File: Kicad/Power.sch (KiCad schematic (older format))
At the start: 29 parts, among them J1 Conn_01x02_Male, J2 Jack-DC, Q1 Q_PMOS_DSG, Q2 Q_NMOS_DSG, U2 LM5155, U3 AMS1117-3.3

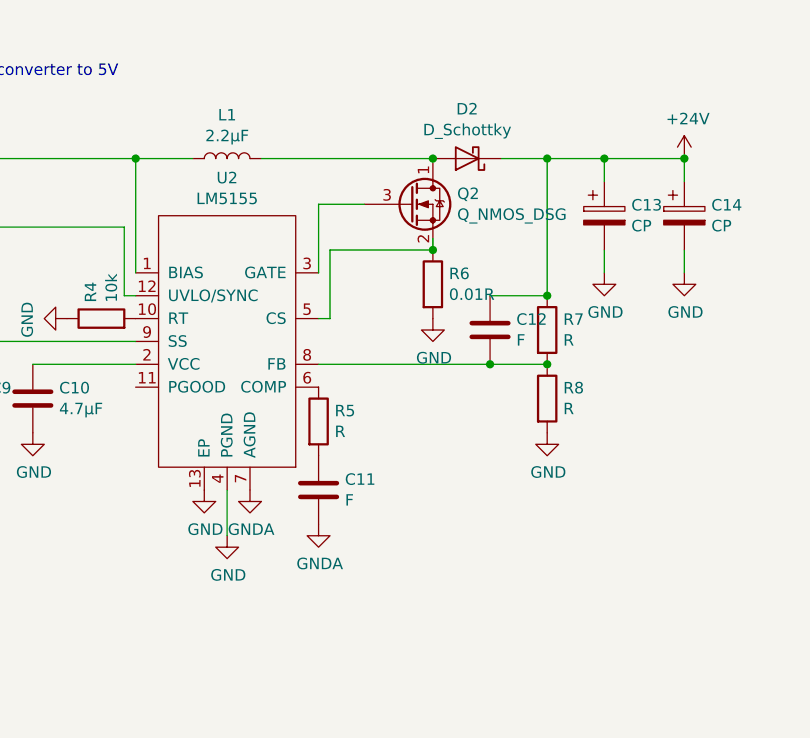
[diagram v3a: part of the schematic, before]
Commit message: Completed the TMC2130 layout and Boost converter layout
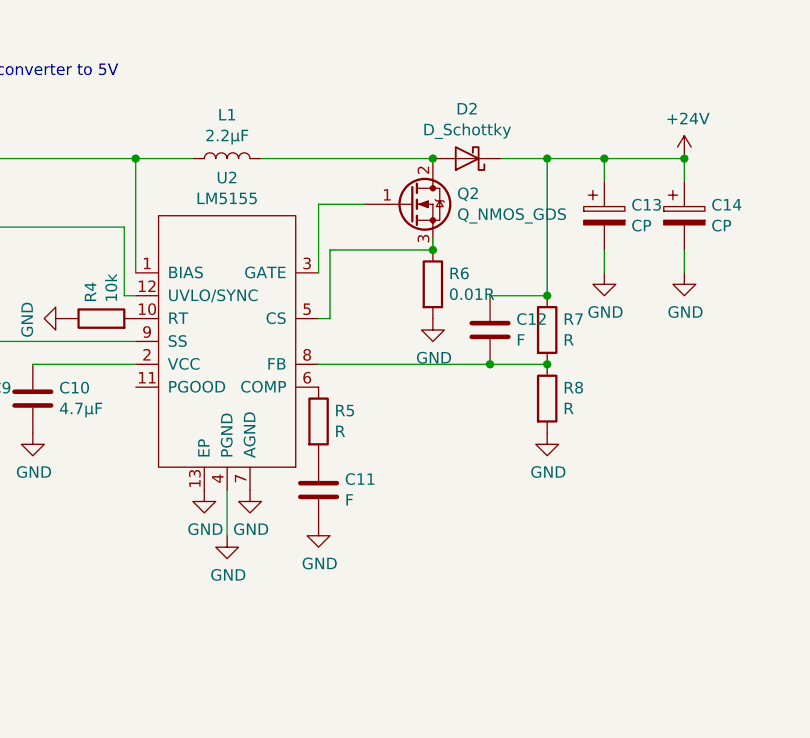
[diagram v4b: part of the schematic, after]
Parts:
- removed Q2: Q_NMOS_DSG, symbol Device:Q_NMOS_DSG
- added Q2: Q_NMOS_GDS, Package_TO_SOT_SMD:TO-252-2, symbol Device:Q_NMOS_GDS
- C10: footprint (none) -> Capacitor_SMD:C_0805_2012Metric
- C11, C12, C9: footprint (none) -> Capacitor_SMD:C_0603_1608Metric
- L1: footprint (none) -> PrivateLib:SRP1265A
- R2, R3, R4, R5, R7, R8: footprint (none) -> Resistor_SMD:R_0603_1608Metric
- R6: footprint (none) -> Resistor_SMD:R_1206_3216Metric
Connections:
- net GNDA is gone; now on net GND: C11.2, U2.7 (AGND)
- net at U2.3 (GATE): now also Q2.1 (G)
- net at R6.1, U2.5 (CS): now also Q2.3 (S)
- net at D2.2 (A), L1.2: now also Q2.2 (D)
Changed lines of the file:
@@
 F 0 "R2" H 4570 3646 50  0000 L CNN
 F 1 "R" H 4570 3555 50  0000 L CNN
-F 2 "" V 4430 3600 50  0001 C CNN
+F 2 "Resistor_SMD:R_0603_1608Metric" V 4430 3600 50  0001 C CNN
 F 3 "~" H 4500 3600 50  0001 C CNN
 	1    4500 3600
@@
 F 0 "R3" H 4570 3946 50  0000 L CNN
 F 1 "R" H 4570 3855 50  0000 L CNN
-F 2 "" V 4430 3900 50  0001 C CNN
+F 2 "Resistor_SMD:R_0603_1608Metric" V 4430 3900 50  0001 C CNN
 F 3 "~" H 4500 3900 50  0001 C CNN
 	1    4500 3900
@@
 F 0 "R4" H 5170 4196 50  0000 L CNN
 F 1 "10k" H 5170 4105 50  0000 L CNN
-F 2 "" V 5030 4150 50  0001 C CNN
+F 2 "Resistor_SMD:R_0603_1608Metric" V 5030 4150 50  0001 C CNN
 F 3 "~" H 5100 4150 50  0001 C CNN
 	1    5100 4150
@@
 F 0 "L1" V 5840 3450 50  0000 C CNN
 F 1 "2.2µF" V 5749 3450 50  0000 C CNN
-F 2 "" H 5650 3450 50  0001 C CNN
+F 2 "PrivateLib:SRP1265A" H 5650 3450 50  0001 C CNN
 F 3 "~" H 5650 3450 50  0001 C CNN
 	1    5650 3450
@@
 	5500 3450 5250 3450
 Connection ~ 5250 3450
-$Comp
-L Device:Q_NMOS_DSG Q2
-U 1 1 5E1E9855
-P 6450 3650
-F 0 "Q2" H 6656 3696 50  0000 L CNN
-F 1 "Q_NMOS_DSG" H 6656 3605 50  0000 L CNN
-F 2 "" H 6650 3750 50  0001 C CNN
-F 3 "~" H 6450 3650 50  0001 C CNN
-	1    6450 3650
-	1    0    0    -1
-$EndComp
 Wire Wire Line
 	6550 3450 5800 3450
@@
 	-1   0    0    1
 $EndComp
-Connection ~ 6550 3450
 $Comp
 L Device:R R6
@@
 F 0 "R6" H 6620 4046 50  0000 L CNN
 F 1 "0.01R" H 6620 3955 50  0000 L CNN
-F 2 "" V 6480 4000 50  0001 C CNN
+F 2 "Resistor_SMD:R_1206_3216Metric" V 6480 4000 50  0001 C CNN
 F 3 "~" H 6550 4000 50  0001 C CNN
 	1    6550 4000
@@
 	1    0    0    -1
 $EndComp
-$Comp
-L power:GNDA #PWR0144
-U 1 1 5E1EFE9C
-P 5750 4900
-F 0 "#PWR0144" H 5750 4650 50  0001 C CNN
-F 1 "GNDA" H 5755 4727 50  0000 C CNN
-F 2 "" H 5750 4900 50  0001 C CNN
-F 3 "" H 5750 4900 50  0001 C CNN
-	1    5750 4900
-	1    0    0    -1
-$EndComp
 Wire Wire Line
 	5650 5100 5650 4900
@@
 F 0 "R5" H 6120 4646 50  0000 L CNN
 F 1 "R" H 6120 4555 50  0000 L CNN
-F 2 "" V 5980 4600 50  0001 C CNN
+F 2 "Resistor_SMD:R_0603_1608Metric" V 5980 4600 50  0001 C CNN
 F 3 "~" H 6050 4600 50  0001 C CNN
 	1    6050 4600
@@
 F 0 "C11" H 6165 4946 50  0000 L CNN
 F 1 "F" H 6165 4855 50  0000 L CNN
-F 2 "" H 6088 4750 50  0001 C CNN
+F 2 "Capacitor_SMD:C_0603_1608Metric" H 6088 4750 50  0001 C CNN
 F 3 "~" H 6050 4900 50  0001 C CNN
 	1    6050 4900
-	1    0    0    -1
-$EndComp
-$Comp
-L power:GNDA #PWR0145
-U 1 1 5E1F1DA4
-P 6050 5050
-F 0 "#PWR0145" H 6050 4800 50  0001 C CNN
-F 1 "GNDA" H 6055 4877 50  0000 C CNN
-F 2 "" H 6050 5050 50  0001 C CNN
-F 3 "" H 6050 5050 50  0001 C CNN
-	1    6050 5050
 	1    0    0    -1
 $EndComp
@@
 F 0 "R7" H 7120 4246 50  0000 L CNN
 F 1 "R" H 7120 4155 50  0000 L CNN
-F 2 "" V 6980 4200 50  0001 C CNN
+F 2 "Resistor_SMD:R_0603_1608Metric" V 6980 4200 50  0001 C CNN
 F 3 "~" H 7050 4200 50  0001 C CNN
 	1    7050 4200
@@
 F 0 "R8" H 7120 4546 50  0000 L CNN
 F 1 "R" H 7120 4455 50  0000 L CNN
-F 2 "" V 6980 4500 50  0001 C CNN
+F 2 "Resistor_SMD:R_0603_1608Metric" V 6980 4500 50  0001 C CNN
 F 3 "~" H 7050 4500 50  0001 C CNN
 	1    7050 4500
@@
 F 0 "C10" H 4915 4546 50  0000 L CNN
 F 1 "4.7µF" H 4915 4455 50  0000 L CNN
-F 2 "" H 4838 4350 50  0001 C CNN
+F 2 "Capacitor_SMD:C_0805_2012Metric" H 4838 4350 50  0001 C CNN
 F 3 "~" H 4800 4500 50  0001 C CNN
 	1    4800 4500
@@
 F 0 "C9" H 4615 4546 50  0000 L CNN
 F 1 "F" H 4615 4455 50  0000 L CNN
-F 2 "" H 4538 4350 50  0001 C CNN
+F 2 "Capacitor_SMD:C_0603_1608Metric" H 4538 4350 50  0001 C CNN
 F 3 "~" H 4500 4500 50  0001 C CNN
 	1    4500 4500
@@
 F 0 "C12" H 6915 4246 50  0000 L CNN
 F 1 "F" H 6915 4155 50  0000 L CNN
-F 2 "" H 6838 4050 50  0001 C CNN
+F 2 "Capacitor_SMD:C_0603_1608Metric" H 6838 4050 50  0001 C CNN
 F 3 "~" H 6800 4200 50  0001 C CNN
 	1    6800 4200
@@
 Connection ~ 4500 3450
 Connection ~ 4250 3450
+$Comp
+L power:GND #PWR0144
+U 1 1 5E2F69BE
+P 5750 4900
+F 0 "#PWR0144" H 5750 4650 50  0001 C CNN
+F 1 "GND" H 5755 4727 50  0000 C CNN
+F 2 "" H 5750 4900 50  0001 C CNN
+F 3 "" H 5750 4900 50  0001 C CNN
+	1    5750 4900
+	1    0    0    -1
+$EndComp
+$Comp
+L power:GND #PWR0145
+U 1 1 5E2FF19C
+P 6050 5050
+F 0 "#PWR0145" H 6050 4800 50  0001 C CNN
+F 1 "GND" H 6055 4877 50  0000 C CNN
+F 2 "" H 6050 5050 50  0001 C CNN
+F 3 "" H 6050 5050 50  0001 C CNN
+	1    6050 5050
+	1    0    0    -1
+$EndComp
+$Comp
+L Device:Q_NMOS_GDS Q2
+U 1 1 5E30B123
+P 6450 3650
+F 0 "Q2" H 6656 3696 50  0000 L CNN
+F 1 "Q_NMOS_GDS" H 6656 3605 50  0000 L CNN
+F 2 "Package_TO_SOT_SMD:TO-252-2" H 6650 3750 50  0001 C CNN
+F 3 "~" H 6450 3650 50  0001 C CNN
+	1    6450 3650
+	1    0    0    -1
+$EndComp
+Connection ~ 6550 3450
 $EndSCHEMATC

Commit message: End of day commit
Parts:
- added U?: MC33063AD, Package_SO:SOIC-8_3.9x4.9mm_P1.27mm, symbol Regulator_Switching:MC33063AD
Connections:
- wire segments 55 -> 57
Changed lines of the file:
@@
 $EndComp
 Connection ~ 6550 3450
+$Comp
+L Regulator_Switching:MC33063AD U?
+U 1 1 5E32E92F
+P 2950 6450
+F 0 "U?" H 2950 6917 50  0000 C CNN
+F 1 "MC33063AD" H 2950 6826 50  0000 C CNN
+F 2 "Package_SO:SOIC-8_3.9x4.9mm_P1.27mm" H 3000 6000 50  0001 L CNN
+F 3 "http://www.onsemi.com/pub_link/Collateral/MC34063A-D.PDF" H 3450 6350 50  0001 C CNN
+	1    2950 6450
+	1    0    0    -1
+$EndComp
+$Comp
+L power:+VDC #PWR?
+U 1 1 5E32F396
+P 2200 6000
+F 0 "#PWR?" H 2200 5900 50  0001 C CNN
+F 1 "+VDC" H 2200 6275 50  0000 C CNN
+F 2 "" H 2200 6000 50  0001 C CNN
+F 3 "" H 2200 6000 50  0001 C CNN
+	1    2200 6000
+	1    0    0    -1
+$EndComp
+Wire Wire Line
+	2200 6000 2200 6250
+Wire Wire Line
+	2200 6250 2550 6250
 $EndSCHEMATC
